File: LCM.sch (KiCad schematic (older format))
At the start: 14 parts

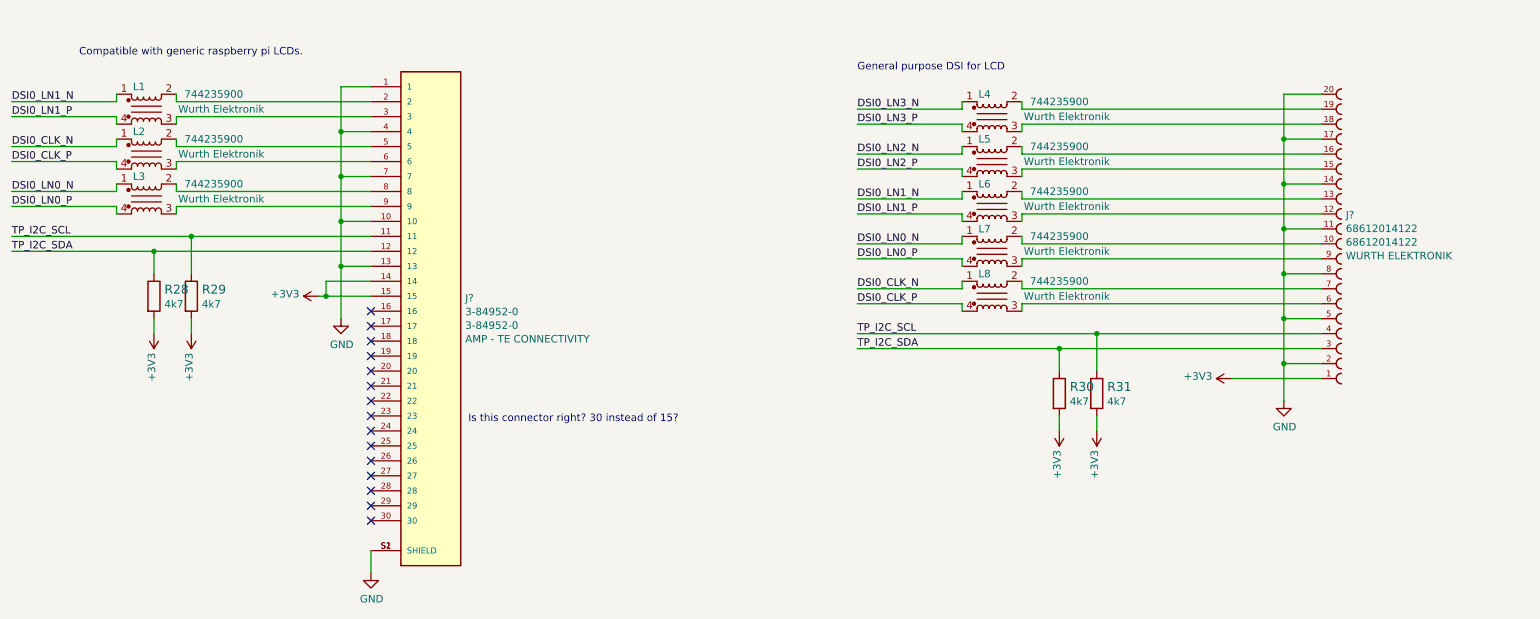
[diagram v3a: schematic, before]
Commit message: added components to pcb and fixed corresponding errors
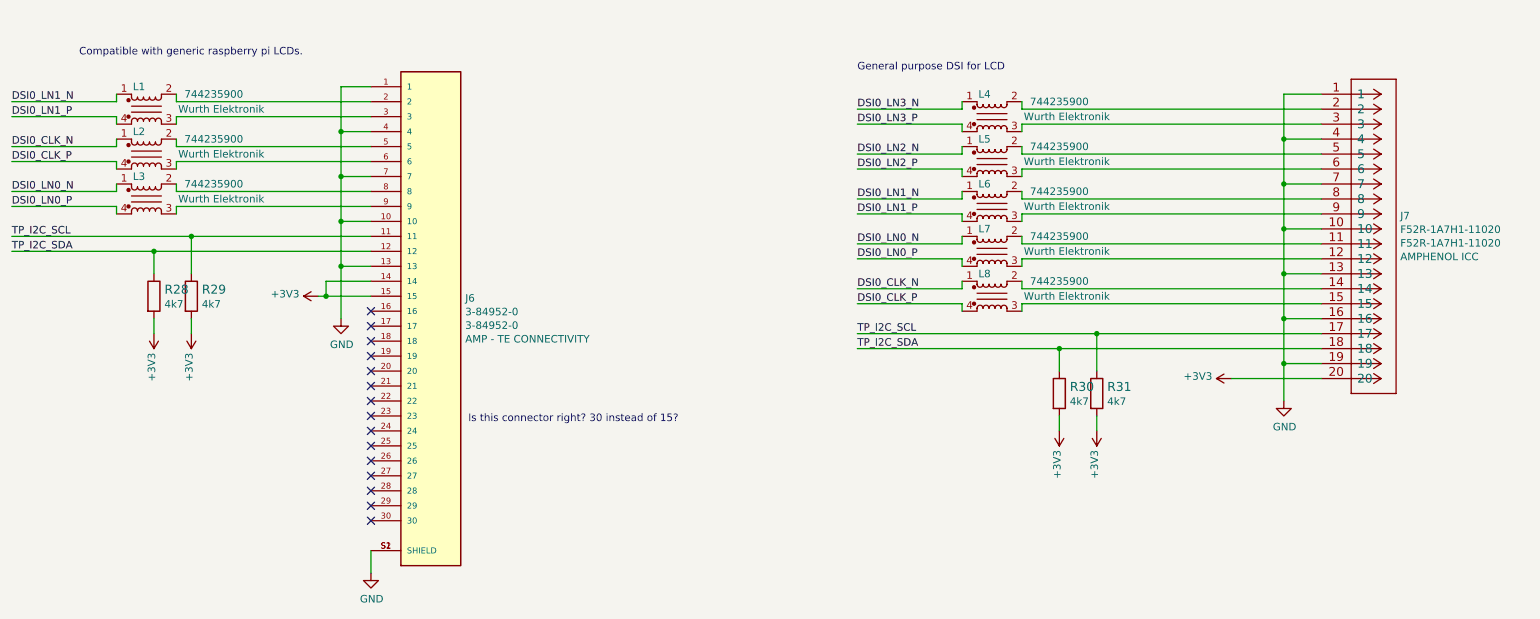
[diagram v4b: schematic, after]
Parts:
- removed J?: 68612014122, antmicro-footprints:68612014122, symbol antmicroFCCConnectors:68612014122
- added J7: F52R-1A7H1-11020, antmicro-footprints:F52R-1A7H1-11020, symbol antmicroFCCConnectors:F52R-1A7H1-11020
- J6: renamed from J?; footprint (none) -> antmicro-footprints:TE_3-84952-0
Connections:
- net +3V3: now also J7.20
- net GND: now also J7.1, J7.10, J7.13, J7.16, J7.19, J7.4, J7.7
- net TP_I2C_SCL: now also J7.17
- net TP_I2C_SDA: now also J7.18
- net at L7.2: now also J7.11
- net at L6.3: now also J7.9
- net at L6.2: now also J7.8
- net at L5.3: now also J7.6
- net at L5.2: now also J7.5
- net at L4.3: now also J7.3
- net at L4.2: now also J7.2
- net at L8.3: now also J7.15
- net at L8.2: now also J7.14
- net at L7.3: now also J7.12
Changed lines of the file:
@@
 	7800 2600 9300 2600
 $Comp
-L antmicroFCCConnectors:68612014122 J?
-U 1 1 61A116F2
-P 9300 2000
-F 0 "J?" H 9464 2193 50  0000 L CNN
-F 1 "68612014122" H 9464 2102 50  0000 L CNN
-F 2 "antmicro-footprints:68612014122" H 10150 2850 50  0001 C CNN
-F 3 "https://www.we-online.com/katalog/datasheet/68612014122.pdf" H 10150 2850 50  0001 C CNN
-F 4 "68612014122" H 9464 2011 50  0000 L CNN "MPN"
-F 5 "WURTH ELEKTRONIK" H 9464 1920 50  0000 L CNN "Manufacturer"
-	1    9300 2000
-	1    0    0    -1
-$EndComp
-$Comp
-L antmicroFCCConnectors:3-84952-0 J?
+L antmicroFCCConnectors:3-84952-0 J6
 U 1 1 619D8F59
 P 3350 2350
-F 0 "J?" H 3580 2337 50  0000 L CNN
+F 0 "J6" H 3580 2337 50  0000 L CNN
 F 1 "3-84952-0" H 3580 2246 50  0000 L CNN
-F 2 "" H 4150 2250 50  0001 L BNN
+F 2 "antmicro-footprints:TE_3-84952-0" H 4150 2250 50  0001 L BNN
 F 3 "https://www.te.com/commerce/DocumentDelivery/DDEController?Action=showdoc&DocId=Data+Sheet%7F1-1773959-6-flexible-printed-circuit-con%7F0919%7Fpdf%7FEnglish%7FENG_DS_1-1773959-6-flexible-printed-circuit-con_0919.pdf%7F3-84952-0" H 4150 2250 50  0001 L BNN
 F 4 "3-84952-0" H 3580 2155 50  0000 L CNN "MPN"
@@
 NoConn ~ 2950 3850
 $Comp
-L power:GND #PWR?
+L power:GND #PWR036
 U 1 1 61A1358A
 P 2950 4200
-F 0 "#PWR?" H 2950 3950 50  0001 C CNN
+F 0 "#PWR036" H 2950 3950 50  0001 C CNN
 F 1 "GND" H 2955 4027 50  0000 C CNN
 F 2 "" H 2950 4200 50  0001 C CNN
@@
 Text Notes 6200 850  0    50   ~ 0
 General purpose DSI for LCD
+$Comp
+L antmicroFCCConnectors:F52R-1A7H1-11020 J7
+U 1 1 61ADF1E8
+P 9500 900
+F 0 "J7" H 9828 -13 50  0000 L CNN
+F 1 "F52R-1A7H1-11020" H 9828 -104 50  0000 L CNN
+F 2 "antmicro-footprints:F52R-1A7H1-11020" H 9500 900 50  0001 C CNN
+F 3 "https://www.snapeda.com/parts/F52R-1A7H1-11020/Amphenol%20ICC%20(FCI)/datasheet/" H 9500 900 50  0001 C CNN
+F 4 "F52R-1A7H1-11020" H 9828 -195 50  0000 L CNN "MPN"
+F 5 "AMPHENOL ICC" H 9828 -286 50  0000 L CNN "Manufacturer"
+	1    9500 900
+	1    0    0    -1
+$EndComp
 $EndSCHEMATC

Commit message: added first version of board layout
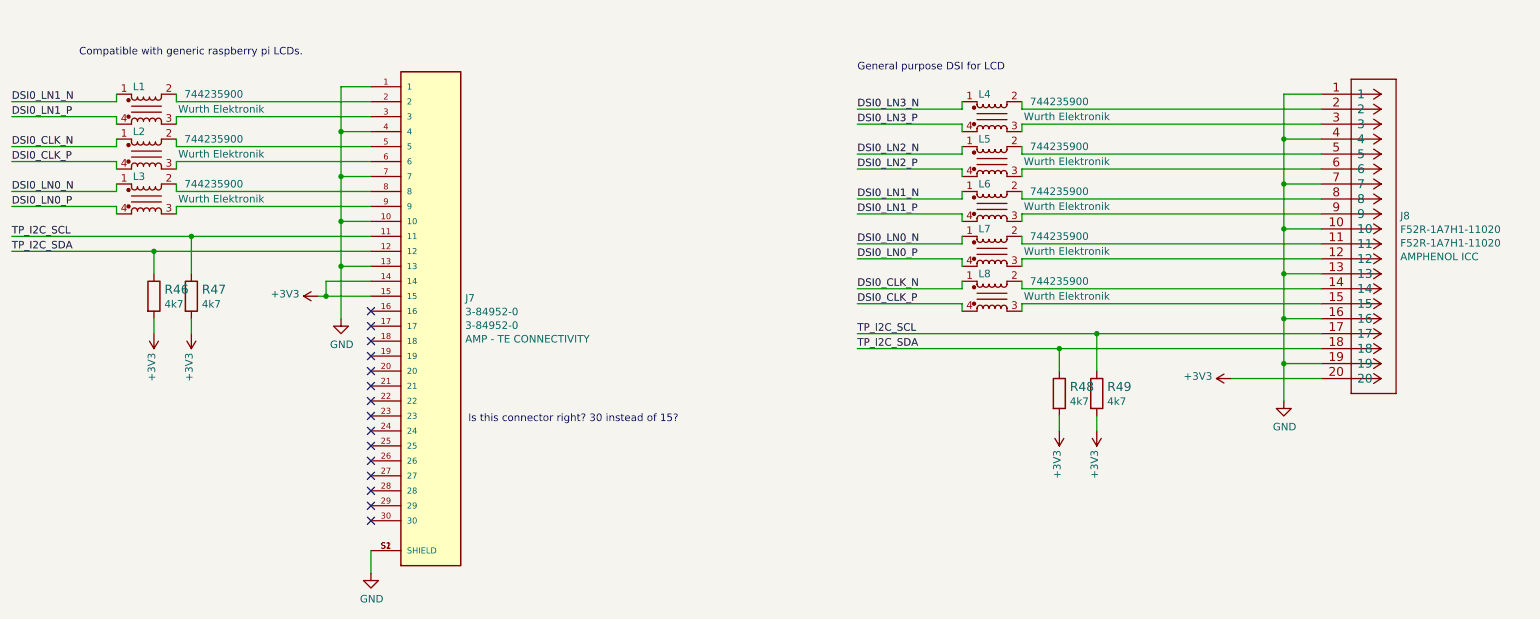
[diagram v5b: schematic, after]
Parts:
- renumbered J6 to J7, J7 to J8, R28 to R46, R29 to R47, R30 to R48, R31 to R49
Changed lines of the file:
@@
 $Descr A3 16535 11693
 encoding utf-8
-Sheet 5 10
+Sheet 5 11
 Title ""
 Date ""
@@
 Connection ~ 2650 2350
 $Comp
-L power:+3V3 #PWR026
+L power:+3V3 #PWR035
 U 1 1 61BD4928
 P 2600 2350
-F 0 "#PWR026" H 2600 2200 50  0001 C CNN
+F 0 "#PWR035" H 2600 2200 50  0001 C CNN
 F 1 "+3V3" V 2615 2478 50  0000 L CNN
 F 2 "" H 2600 2350 50  0001 C CNN
@@
 Connection ~ 2750 2150
 $Comp
-L power:GND #PWR027
+L power:GND #PWR036
 U 1 1 61BD6C0B
 P 2750 2500
-F 0 "#PWR027" H 2750 2250 50  0001 C CNN
+F 0 "#PWR036" H 2750 2250 50  0001 C CNN
 F 1 "GND" H 2755 2327 50  0000 C CNN
 F 2 "" H 2750 2500 50  0001 C CNN
@@
 Connection ~ 9050 2500
 $Comp
-L power:+3V3 #PWR028
+L power:+3V3 #PWR040
 U 1 1 61BE8457
 P 8700 2900
-F 0 "#PWR028" H 8700 2750 50  0001 C CNN
+F 0 "#PWR040" H 8700 2750 50  0001 C CNN
 F 1 "+3V3" V 8715 3028 50  0000 L CNN
 F 2 "" H 8700 2900 50  0001 C CNN
@@
 Connection ~ 9050 2800
 $Comp
-L power:GND #PWR029
+L power:GND #PWR041
 U 1 1 61BEA7A9
 P 9050 3050
-F 0 "#PWR029" H 9050 2800 50  0001 C CNN
+F 0 "#PWR041" H 9050 2800 50  0001 C CNN
 F 1 "GND" H 9055 2877 50  0000 C CNN
 F 2 "" H 9050 3050 50  0001 C CNN
@@
 	6200 2700 7550 2700
 $Comp
-L antmicroResistors0402:R_4k7_0402 R29
+L antmicroResistors0402:R_4k7_0402 R47
 U 1 1 619BC4E7
 P 1750 2350
-F 0 "R29" V 1705 2420 60  0000 L CNN
+F 0 "R47" V 1705 2420 60  0000 L CNN
 F 1 "R_4k7_0402" H 1750 2200 60  0001 C CNN
 F 2 "antmicro-footprints:0402-res" H 1950 2550 60  0001 L CNN
@@
 $EndComp
 $Comp
-L antmicroResistors0402:R_4k7_0402 R28
+L antmicroResistors0402:R_4k7_0402 R46
 U 1 1 619BDFE3
 P 1500 2350
-F 0 "R28" V 1455 2420 60  0000 L CNN
+F 0 "R46" V 1455 2420 60  0000 L CNN
 F 1 "R_4k7_0402" H 1500 2200 60  0001 C CNN
 F 2 "antmicro-footprints:0402-res" H 1700 2550 60  0001 L CNN
@@
 	1500 2500 1500 2600
 $Comp
-L power:+3V3 #PWR030
+L power:+3V3 #PWR033
 U 1 1 619CDB8C
 P 1500 2600
-F 0 "#PWR030" H 1500 2450 50  0001 C CNN
+F 0 "#PWR033" H 1500 2450 50  0001 C CNN
 F 1 "+3V3" V 1515 2728 50  0000 L CNN
 F 2 "" H 1500 2600 50  0001 C CNN
@@
 $EndComp
 $Comp
-L power:+3V3 #PWR031
+L power:+3V3 #PWR034
 U 1 1 619CE012
 P 1750 2600
-F 0 "#PWR031" H 1750 2450 50  0001 C CNN
+F 0 "#PWR034" H 1750 2450 50  0001 C CNN
 F 1 "+3V3" V 1765 2728 50  0000 L CNN
 F 2 "" H 1750 2600 50  0001 C CNN
@@
 $EndComp
 $Comp
-L antmicroResistors0402:R_4k7_0402 R31
+L antmicroResistors0402:R_4k7_0402 R49
 U 1 1 619D2E39
 P 7800 3000
-F 0 "R31" V 7755 3070 60  0000 L CNN
+F 0 "R49" V 7755 3070 60  0000 L CNN
 F 1 "R_4k7_0402" H 7800 2850 60  0001 C CNN
 F 2 "antmicro-footprints:0402-res" H 8000 3200 60  0001 L CNN
@@
 $EndComp
 $Comp
-L antmicroResistors0402:R_4k7_0402 R30
+L antmicroResistors0402:R_4k7_0402 R48
 U 1 1 619D2E42
 P 7550 3000
-F 0 "R30" V 7505 3070 60  0000 L CNN
+F 0 "R48" V 7505 3070 60  0000 L CNN
 F 1 "R_4k7_0402" H 7550 2850 60  0001 C CNN
 F 2 "antmicro-footprints:0402-res" H 7750 3200 60  0001 L CNN
@@
 	7550 3150 7550 3250
 $Comp
-L power:+3V3 #PWR032
+L power:+3V3 #PWR038
 U 1 1 619D2E4C
 P 7550 3250
-F 0 "#PWR032" H 7550 3100 50  0001 C CNN
+F 0 "#PWR038" H 7550 3100 50  0001 C CNN
 F 1 "+3V3" V 7565 3378 50  0000 L CNN
 F 2 "" H 7550 3250 50  0001 C CNN
@@
 $EndComp
 $Comp
-L power:+3V3 #PWR033
+L power:+3V3 #PWR039
 U 1 1 619D2E52
 P 7800 3250
-F 0 "#PWR033" H 7800 3100 50  0001 C CNN
+F 0 "#PWR039" H 7800 3100 50  0001 C CNN
 F 1 "+3V3" V 7815 3378 50  0000 L CNN
 F 2 "" H 7800 3250 50  0001 C CNN
@@
 	7800 2600 9300 2600
 $Comp
-L antmicroFCCConnectors:3-84952-0 J6
+L antmicroFCCConnectors:3-84952-0 J7
 U 1 1 619D8F59
 P 3350 2350
-F 0 "J6" H 3580 2337 50  0000 L CNN
+F 0 "J7" H 3580 2337 50  0000 L CNN
 F 1 "3-84952-0" H 3580 2246 50  0000 L CNN
 F 2 "antmicro-footprints:TE_3-84952-0" H 4150 2250 50  0001 L BNN
@@
 NoConn ~ 2950 3850
 $Comp
-L power:GND #PWR036
+L power:GND #PWR037
 U 1 1 61A1358A
 P 2950 4200
-F 0 "#PWR036" H 2950 3950 50  0001 C CNN
+F 0 "#PWR037" H 2950 3950 50  0001 C CNN
 F 1 "GND" H 2955 4027 50  0000 C CNN
 F 2 "" H 2950 4200 50  0001 C CNN
@@
 General purpose DSI for LCD
 $Comp
-L antmicroFCCConnectors:F52R-1A7H1-11020 J7
+L antmicroFCCConnectors:F52R-1A7H1-11020 J8
 U 1 1 61ADF1E8
 P 9500 900
-F 0 "J7" H 9828 -13 50  0000 L CNN
+F 0 "J8" H 9828 -13 50  0000 L CNN
 F 1 "F52R-1A7H1-11020" H 9828 -104 50  0000 L CNN
 F 2 "antmicro-footprints:F52R-1A7H1-11020" H 9500 900 50  0001 C CNN

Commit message: replaced common mode chokes, dedicated for hdmi and with smaller footprint
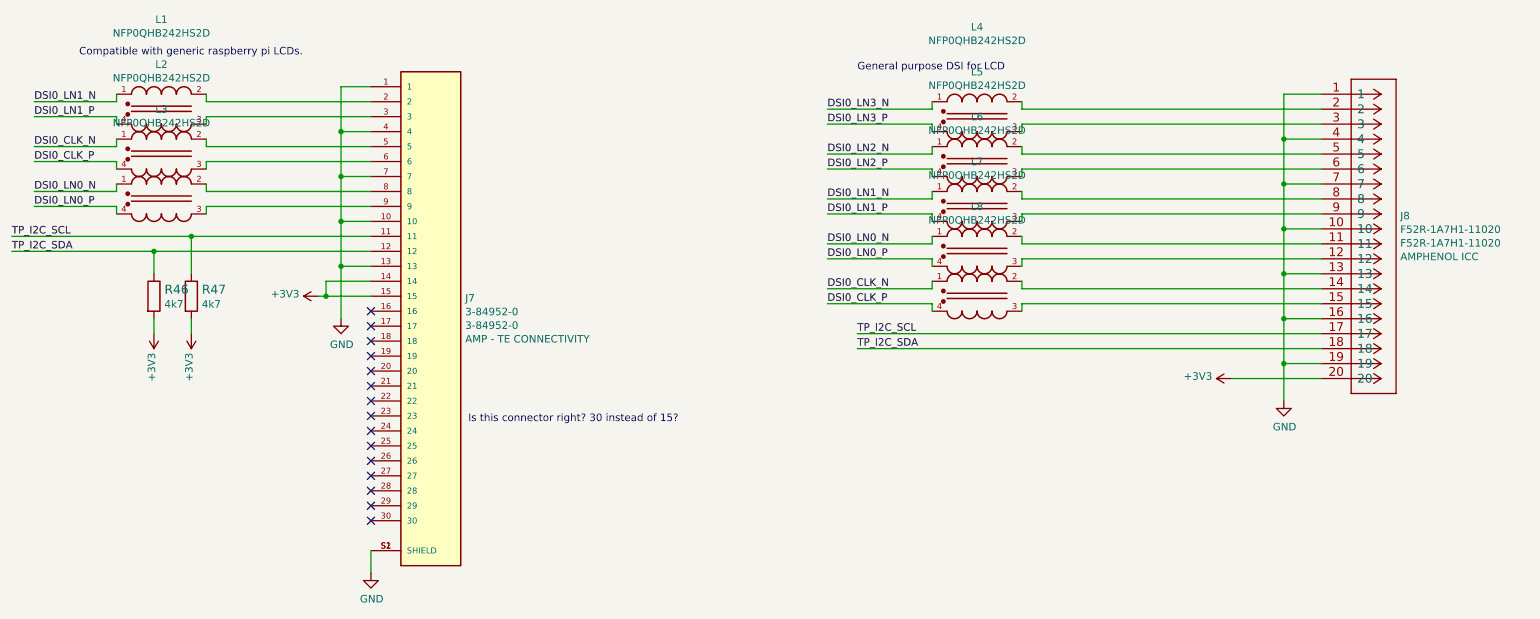
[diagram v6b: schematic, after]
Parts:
- removed L1, L2, L3, L4, L5, L6, L7, L8: 744235900, antmicro-footprints:744235900, symbol antmicroFixedInductors:744235900
- removed R48, R49: R_4k7_0402, antmicro-footprints:0402-res, symbol antmicroResistors0402:R_4k7_0402
- added L1, L2, L3, L4, L5, L6, L7, L8: NFP0QHB242HS2D, antmicro-footprints:FIL_NFP0QHB242HS2D, symbol antmicroFixedInductors:NFP0QHB242HS2D
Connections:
- net DSI0_CLK_N: now also L2.1, L8.1
- net DSI0_CLK_P: now also L2.4, L8.4
- net DSI0_LN0_N: now also L3.1, L7.1
- net DSI0_LN0_P: now also L3.4, L7.4
- net DSI0_LN1_N: now also L1.1, L6.1
- net DSI0_LN1_P: now also L1.4, L6.4
- net DSI0_LN2_N: now also L5.1
- net DSI0_LN2_P: now also L5.4
- net DSI0_LN3_N: now also L4.1
- net DSI0_LN3_P: now also L4.4
- net at J7.2: now also L1.2
- net at J7.3: now also L1.3
- net at J7.5: now also L2.2
- net at J7.6: now also L2.3
- net at J7.8: now also L3.2
- net at J7.9: now also L3.3
- net at J8.11: now also L7.2
- net at J8.12: now also L7.3
- net at J8.14: now also L8.2
- net at J8.15: now also L8.3
- net at J8.2: now also L4.2
- net at J8.3: now also L4.3
- net at J8.5: now also L5.2
- net at J8.6: now also L5.3
- net at J8.8: now also L6.2
- net at J8.9: now also L6.3

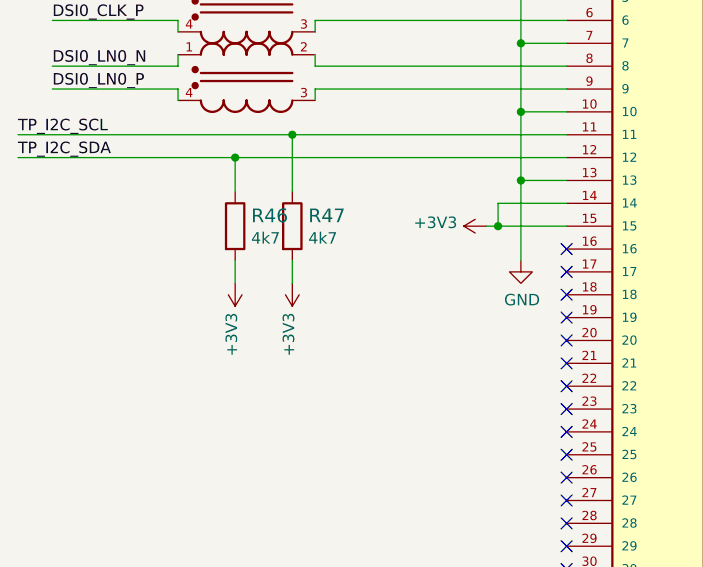
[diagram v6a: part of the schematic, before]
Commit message: changed arrangement of hierarchical sheets
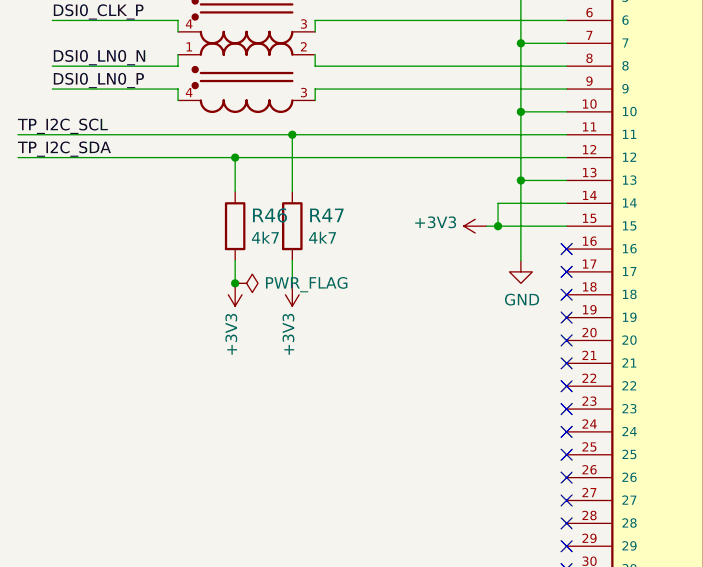
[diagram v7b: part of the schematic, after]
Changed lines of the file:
@@
 Wire Wire Line
 	6200 2700 9300 2700
+$Comp
+L power:PWR_FLAG #FLG0102
+U 1 1 62BD2011
+P 1500 2600
+F 0 "#FLG0102" H 1500 2675 50  0001 C CNN
+F 1 "PWR_FLAG" V 1500 2728 50  0000 L CNN
+F 2 "" H 1500 2600 50  0001 C CNN
+F 3 "~" H 1500 2600 50  0001 C CNN
+	1    1500 2600
+	0    1    1    0
+$EndComp
+Connection ~ 1500 2600
 $EndSCHEMATC
